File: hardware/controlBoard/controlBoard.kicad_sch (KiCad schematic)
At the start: 36 parts, among them J1 Conn_01x10_Pin, J2 USB_C_Receptacle_USB2.0_14P, T1 BC847, T2 BC847, U2 LM1117DT-3.3, U3 CH340G, U4 DS3231M, U5 ESP32-WROOM-32D, Y2 405I35D25M00000

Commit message: Finalize PCB design
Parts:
- Y2: value 405I35D25M00000 -> 12MHz
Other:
- moved on the sheet: C10, C5, C6, C7, C9, R12, R14, R6, R7, T1, T2, U3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

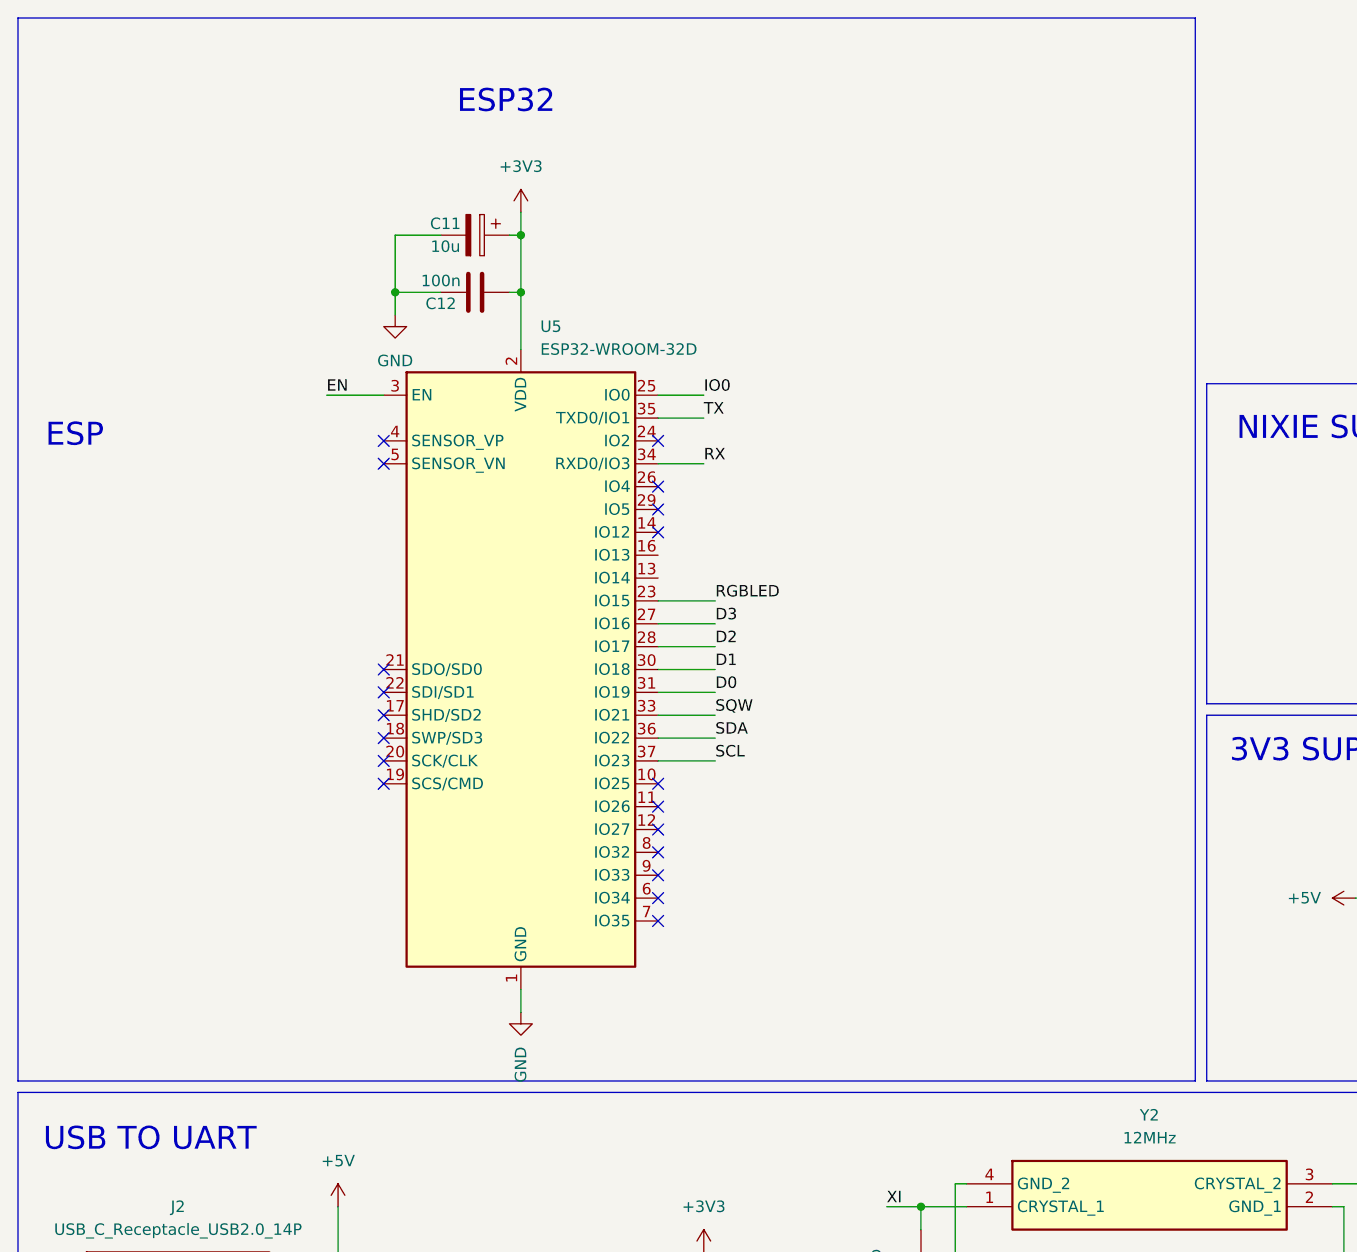
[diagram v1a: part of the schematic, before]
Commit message: Cosmetic fix on control board schematic
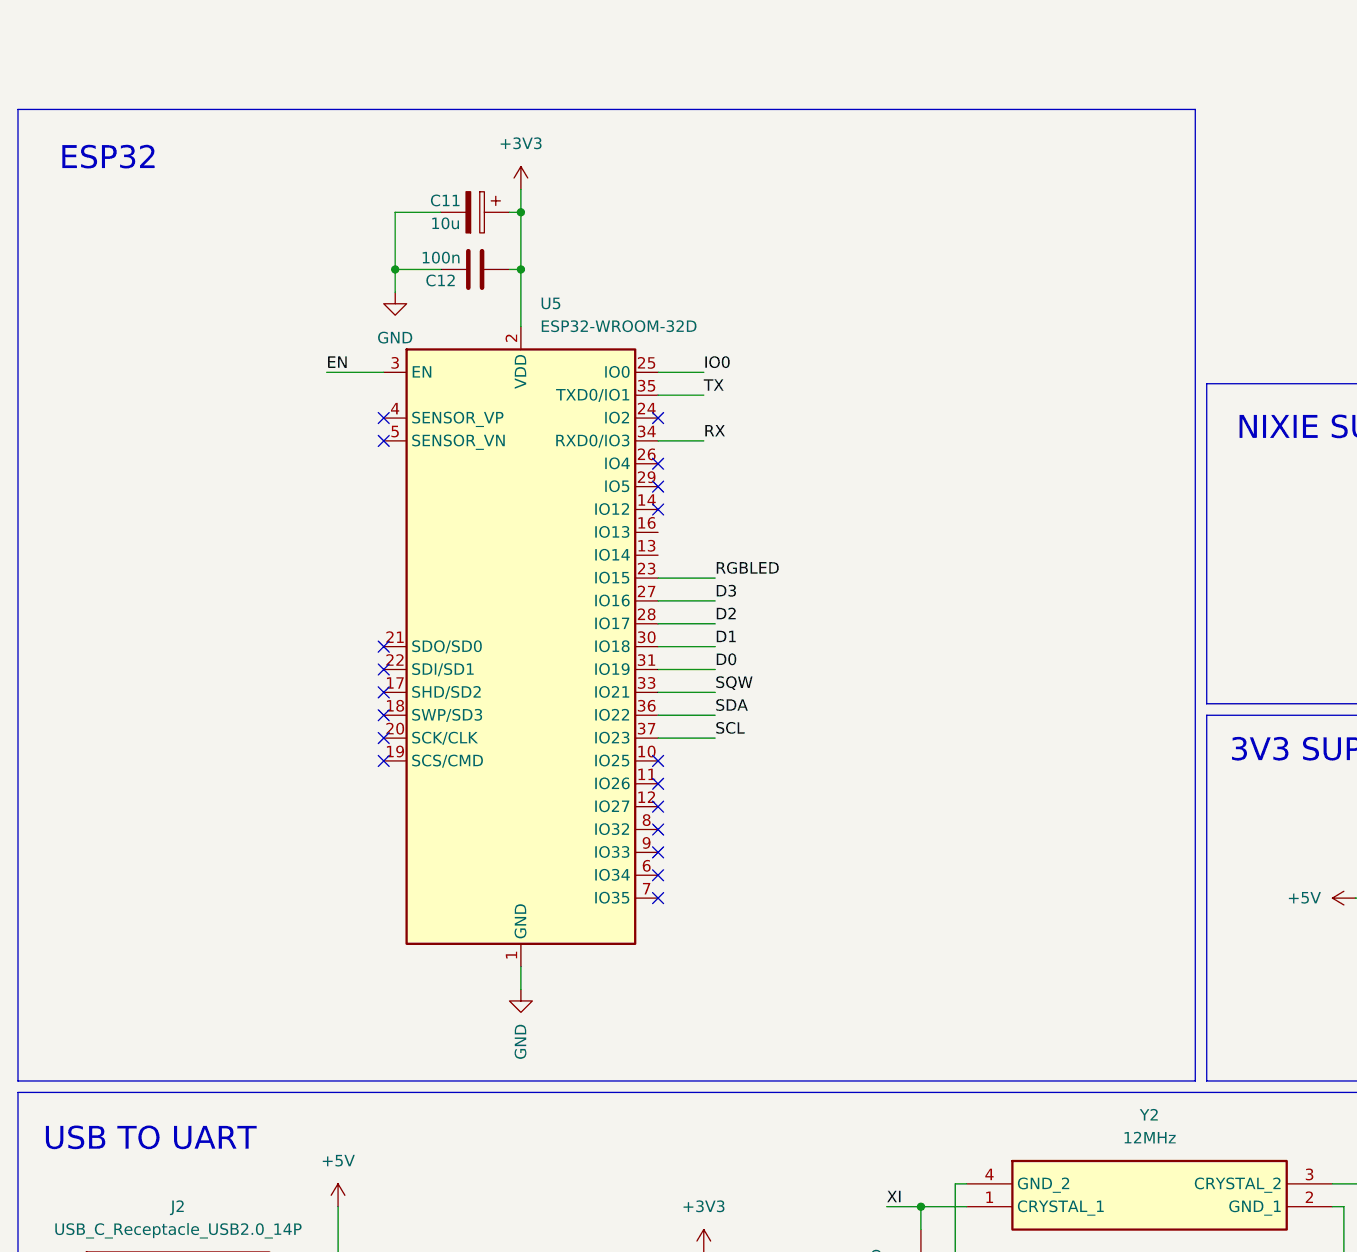
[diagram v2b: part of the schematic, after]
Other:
- note removed: "ESP"
- moved on the sheet: C11, C12, U5

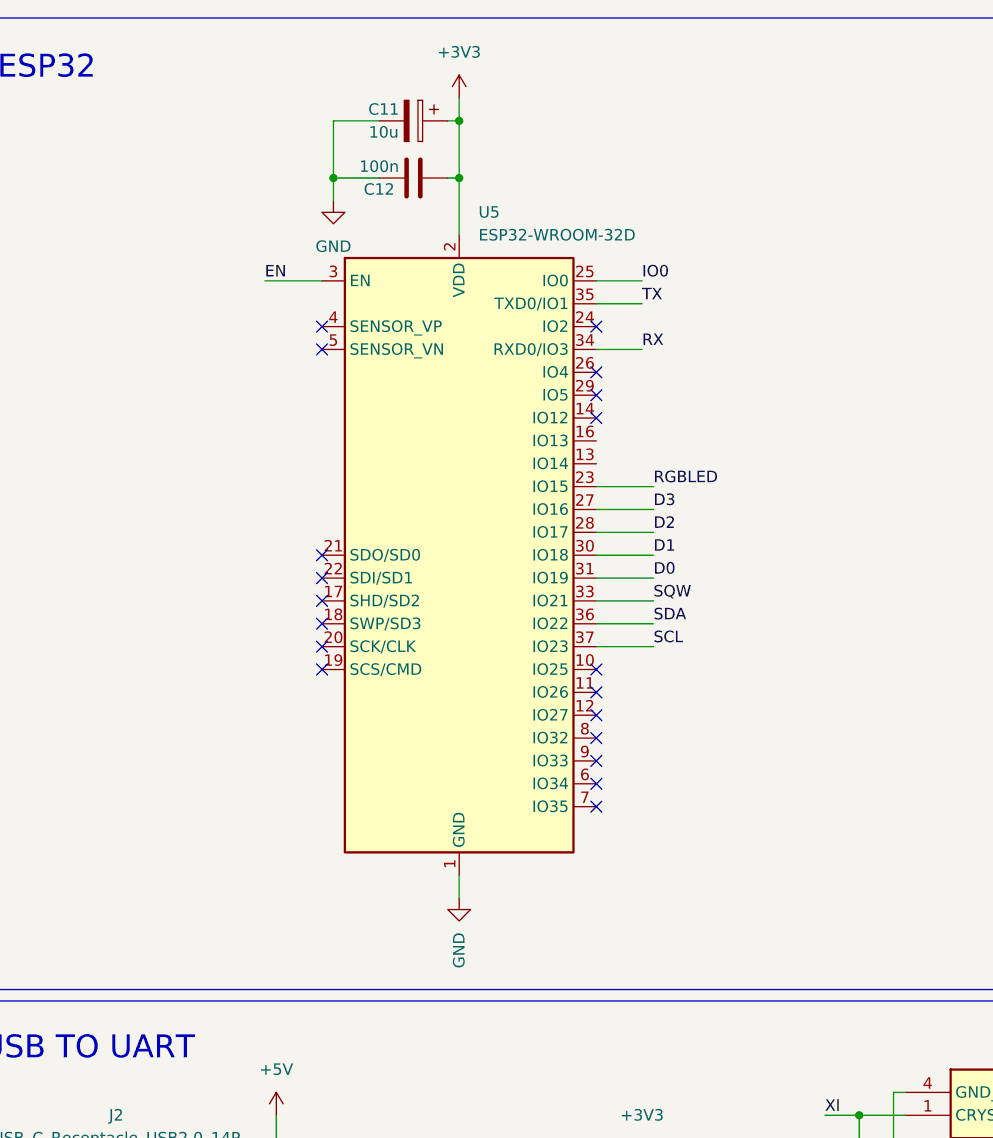
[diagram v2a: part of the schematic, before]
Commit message: Fix auto-programming circuit issue
- Add pullups to EN and IO0 pins.
- Add 100nF ceramic capacitor between EN and GND to improve timimng.
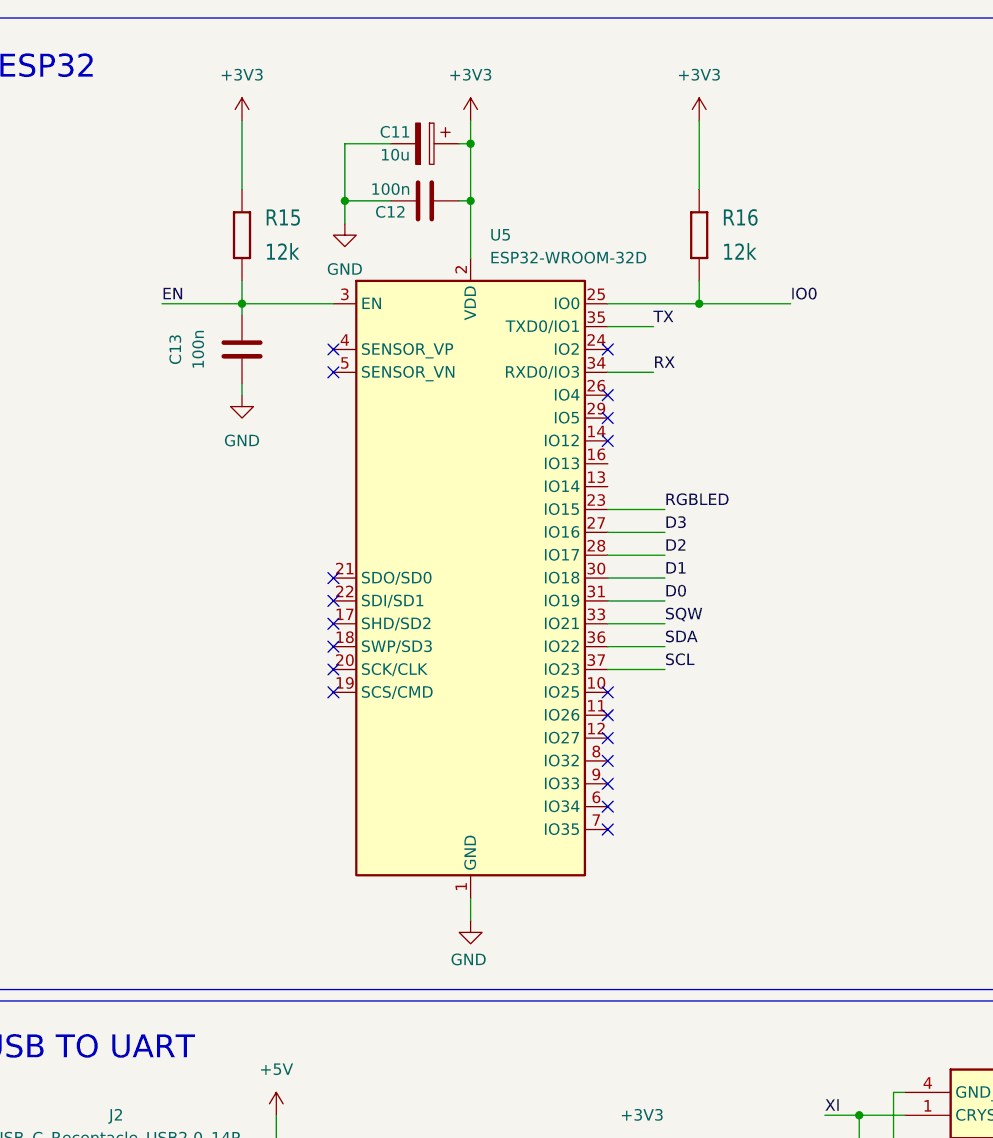
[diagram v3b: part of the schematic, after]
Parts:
- added C13: 100n, Capacitor_SMD:C_0603_1608Metric, symbol Device:C
- added R15, R16: 12k, Resistor_SMD:R_0603_1608Metric, symbol controlBoard-eagle-import:R-EU_R0603
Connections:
- net +3V3: now also R15.2, R16.2
- net EN: now also C13.1, R15.1
- net GND: now also C13.2
- net IO0: now also R16.1
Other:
- moved on the sheet: C11, C12, U5
